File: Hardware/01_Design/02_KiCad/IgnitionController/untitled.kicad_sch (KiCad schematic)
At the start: 34 parts, among them Q4 PMOS-FET, Q5 BC856, Q6 IRF9Z34NSPbF, U3 LM2575-3.3BU, U4 LM2575-5.0BU, U9 LM2575-5.0BU

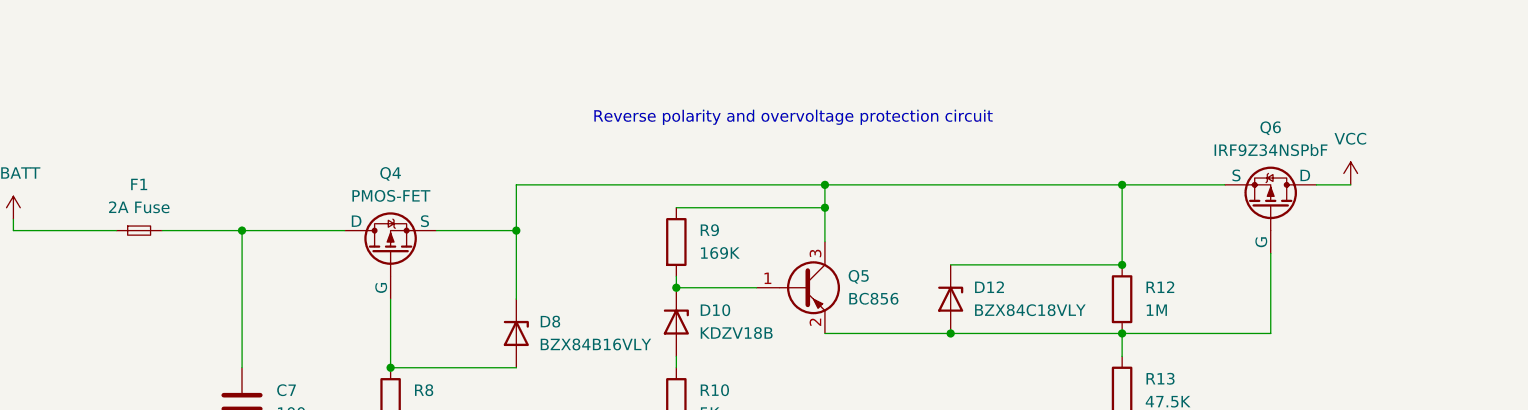
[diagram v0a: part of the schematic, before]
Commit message: Added Crystal to PMIC
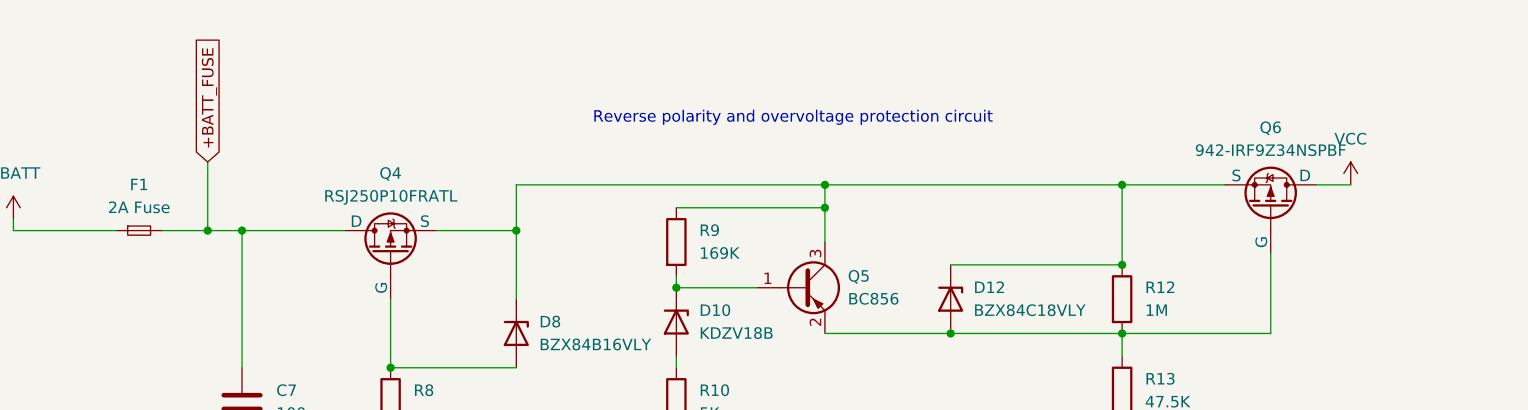
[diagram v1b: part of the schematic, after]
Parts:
- removed Q6: IRF9Z34NSPbF, Package_TO_SOT_SMD:TO-263-2, symbol Simulation_SPICE:PMOS
- added Q6: 942-IRF9Z34NSPBF, Library:TO-263-2_Transistor, symbol Library_sym.pretty:PMOS-FET
- C7: footprint Capacitor_SMD:C_0805_2012Metric_Pad1.18x1.45mm_HandSolder -> Capacitor_SMD:C_0603_1608Metric_Pad1.08x0.95mm_HandSolder
- Q4: value PMOS-FET -> RSJ250P10FRATL; Mouser PN (none) -> 755-RSJ250P10FRATL
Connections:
- net VCC: now also Q6.2 (D)
- net +BATT_FUSE: now reaches C7.1, F1.2, Q4.2 (D)
- net at D12.3 (K), D8.3 (K), Q4.3 (S)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: now also Q6.3 (S)
- net at D12.1 (A), Q5.2 (E), R12.2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: now also Q6.1 (G)
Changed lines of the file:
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@@
 	)
 	(junction
+		(at 67.31 53.34)
+		(diameter 0)
+		(color 0 0 0 0)
+	)
+	(junction
 		(at 168.91 57.15)
 		(diameter 0)
@@
 	(wire
 		(pts
+			(xy 67.31 53.34) (xy 62.23 53.34)
+		)
+		(stroke
+			(width 0)
+			(type default)
+		)
+	)
+	(wire
+		(pts
 			(xy 80.01 107.95) (xy 86.36 107.95)
 		)
@@
 	(wire
 		(pts
+			(xy 67.31 45.72) (xy 67.31 53.34)
+		)
+		(stroke
+			(width 0)
+			(type default)
+		)
+	)
+	(wire
+		(pts
 			(xy 31.75 111.76) (xy 31.75 115.57)
 		)
@@
 	(wire
 		(pts
-			(xy 71.12 53.34) (xy 62.23 53.34)
+			(xy 71.12 53.34) (xy 67.31 53.34)
 		)
 		(stroke
@@
 		)
 	)
+	(global_label "+BATT_FUSE"
+		(shape input)
+		(at 67.31 45.72 90)
+		(fields_autoplaced yes)
+		(effects
+			(font
+				(size 1.27 1.27)
+			)
+			(justify left)
+		)
+		(property "Intersheetrefs" "${INTERSHEET_REFS}"
+			(at 67.31 31.1234 90)
+			(effects
+				(font
+					(size 1.27 1.27)
+				)
+				(justify left)
+				(hide yes)
+			)
+		)
+	)
 	(symbol
 		(lib_id "Device:D_Zener")
@@
 			)
 		)
-		(property "Value" "PMOS-FET"
+		(property "Value" "RSJ250P10FRATL"
 			(at 87.63 49.53 90)
 			(effects
@@
 			)
 		)
+		(property "Mouser PN" "755-RSJ250P10FRATL"
+			(at 87.63 55.88 90)
+			(effects
+				(font
+					(size 1.27 1.27)
+				)
+				(hide yes)
+			)
+		)
 		(pin "3"
 		)
@@
 			)
 		)
-		(property "Footprint" "Capacitor_SMD:C_0805_2012Metric_Pad1.18x1.45mm_HandSolder"
+		(property "Footprint" "Capacitor_SMD:C_0603_1608Metric_Pad1.08x0.95mm_HandSolder"
 			(at 72.0852 76.2 0)
 			(effects
@@
 	)
 	(symbol
-		(lib_id "Simulation_SPICE:PMOS")
-		(at 185.42 50.8 270)
-		(mirror x)
-		(unit 1)
-		(exclude_from_sim no)
-		(in_bom yes)
-		(on_board yes)
-		(dnp no)
-		(property "Reference" "Q6"
-			(at 185.42 41.91 90)
-			(effects
-				(font
-					(size 1.27 1.27)
-				)
-			)
-		)
-		(property "Value" "IRF9Z34NSPbF"
-			(at 185.42 44.45 90)
-			(effects
-				(font
-					(size 1.27 1.27)
-				)
-			)
-		)
-		(property "Footprint" "Package_TO_SOT_SMD:TO-263-2"
-			(at 187.96 45.72 0)
-			(effects
-				(font
-					(size 1.27 1.27)
-				)
-				(hide yes)
-			)
-		)
-		(property "Datasheet" "https://ngspice.sourceforge.io/docs/ngspice-html-manual/manual.xhtml#cha_MOSFETs"
-			(at 172.72 50.8 0)
-			(effects
-				(font
-					(size 1.27 1.27)
-				)
-				(hide yes)
-			)
-		)
-		(property "Description" "P-MOSFET transistor, drain/source/gate"
-			(at 185.42 50.8 0)
-			(effects
-				(font
-					(size 1.27 1.27)
-				)
-				(hide yes)
-			)
-		)
-		(property "Sim.Device" "PMOS"
-			(at 168.275 50.8 0)
-			(effects
-				(font
-					(size 1.27 1.27)
-				)
-				(hide yes)
-			)
-		)
-		(property "Sim.Type" "VDMOS"
-			(at 166.37 50.8 0)
-			(effects
-				(font
-					(size 1.27 1.27)
-				)
-				(hide yes)
-			)
-		)
-		(property "Sim.Pins" "1=D 2=G 3=S"
-			(at 170.18 50.8 0)
-			(effects
-				(font
-					(size 1.27 1.27)
-				)
-				(hide yes)
-			)
-		)
-		(pin "2"
-		)
-		(pin "1"
-		)
-		(pin "3"
-		)
-		(instances
-			(project "IgnitionController"
-				(path "/96744ec0-1e7f-4d75-9985-0095978419e2/af36972c-908c-4a23-b0c1-8f51d47880c3"
-					(reference "Q6")
-					(unit 1)
-				)
-			)
-		)
-	)
-	(symbol
 		(lib_id "Diode:SS14")
 		(at 82.55 160.02 270)
@@
 					(unit 1)
 				)
+			)
+		)
+	)
+	(symbol
+		(lib_id "Library_sym.pretty:PMOS-FET")
+		(at 185.42 50.8 270)
+		(mirror x)
+		(unit 1)
+		(exclude_from_sim no)
+		(in_bom yes)
+		(on_board yes)
+		(dnp no)
+		(property "Reference" "Q6"
+			(at 185.42 41.91 90)
+			(effects
+				(font
+					(size 1.27 1.27)
+				)
+			)
+		)
+		(property "Value" "942-IRF9Z34NSPBF"
+			(at 185.42 44.45 90)
+			(effects
+				(font
+					(size 1.27 1.27)
+				)
+			)
+		)
+		(property "Footprint" "Library:TO-263-2_Transistor"
+			(at 187.96 45.72 0)
+			(effects
+				(font
+					(size 1.27 1.27)
+				)
+				(hide yes)
+			)
+		)
+		(property "Datasheet" "https://ngspice.sourceforge.io/docs/ngspice-html-manual/manual.xhtml#cha_MOSFETs"
+			(at 172.72 50.8 0)
+			(effects
+				(font
+					(size 1.27 1.27)
+				)
+				(hide yes)
+			)
+		)
+		(property "Description" "P-MOSFET transistor, drain/source/gate"
+			(at 185.42 50.8 0)
+			(effects
+				(font
+					(size 1.27 1.27)
+				)
+				(hide yes)
+			)
+		)
+		(property "Sim.Device" "PMOS"
+			(at 168.275 50.8 0)
+			(effects
+				(font
+					(size 1.27 1.27)
+				)
+				(hide yes)
+			)
+		)
+		(property "Sim.Type" "VDMOS"
+			(at 166.37 50.8 0)
+			(effects
+				(font
+					(size 1.27 1.27)
+				)
+				(hide yes)
+			)
+		)
+		(property "Sim.Pins" "1=D 2=G 3=S"
+			(at 170.18 50.8 0)
+			(effects
+				(font
+					(size 1.27 1.27)
+				)
+				(hide yes)
+			)
+		)
+		(property "Mouser PN" ""
+			(at 185.42 50.8 90)
+			(effects
+				(font
+					(size 1.27 1.27)
+				)
+				(hide yes)
+			)
+		)
+		(pin "3"
+		)
+		(pin "1"
+		)
+		(pin "2"
+		)
+		(instances
+			(project "IgnitionController"
+				(path "/96744ec0-1e7f-4d75-9985-0095978419e2/af36972c-908c-4a23-b0c1-8f51d47880c3"
+					(reference "Q6")
+					(unit 1)
+				)

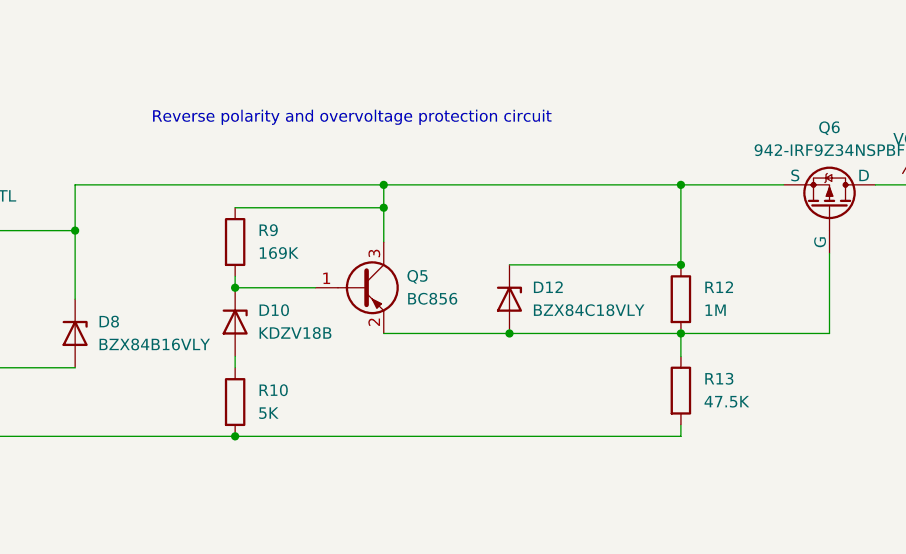
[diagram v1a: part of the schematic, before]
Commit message: Added Peripheral HW Components
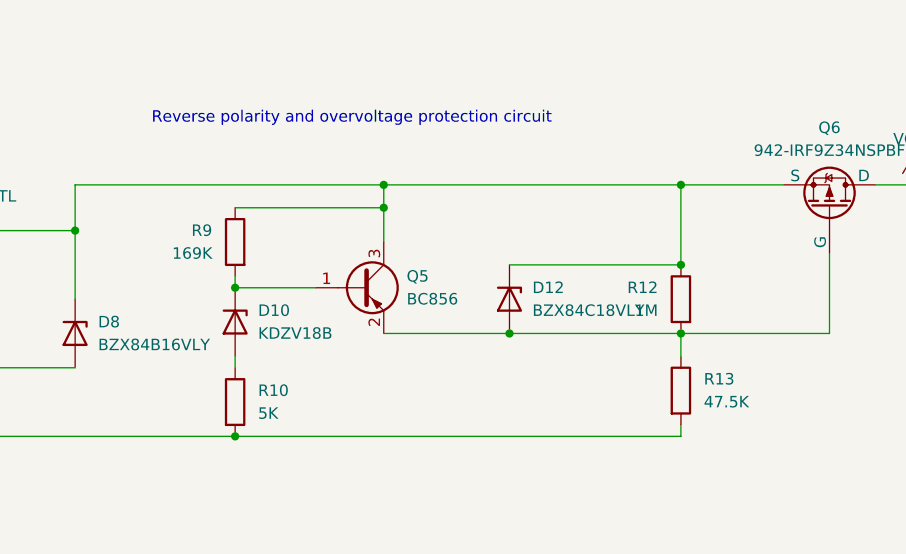
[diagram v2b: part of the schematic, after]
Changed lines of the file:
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@@
 		(lib_id "Device:R")
 		(at 168.91 60.96 0)
-		(unit 1)
-		(exclude_from_sim no)
-		(in_bom yes)
-		(on_board yes)
-		(dnp no)
-		(fields_autoplaced yes)
+		(mirror y)
+		(unit 1)
+		(exclude_from_sim no)
+		(in_bom yes)
+		(on_board yes)
+		(dnp no)
 		(property "Reference" "R12"
-			(at 171.45 59.6899 0)
+			(at 166.37 59.6899 0)
 			(effects
 				(font
@@
 		)
 		(property "Value" "1M"
-			(at 171.45 62.2299 0)
+			(at 166.37 62.2299 0)
 			(effects
 				(font
@@
 		)
 		(property "Footprint" "Resistor_SMD:R_0603_1608Metric_Pad0.98x0.95mm_HandSolder"
-			(at 167.132 60.96 90)
+			(at 170.688 60.96 90)
 			(effects
 				(font
@@
 		(lib_id "Device:R")
 		(at 119.38 54.61 0)
-		(unit 1)
-		(exclude_from_sim no)
-		(in_bom yes)
-		(on_board yes)
-		(dnp no)
-		(fields_autoplaced yes)
+		(mirror y)
+		(unit 1)
+		(exclude_from_sim no)
+		(in_bom yes)
+		(on_board yes)
+		(dnp no)
 		(property "Reference" "R9"
-			(at 121.92 53.3399 0)
+			(at 116.84 53.3399 0)
 			(effects
 				(font
@@
 		)
 		(property "Value" "169K"
-			(at 121.92 55.8799 0)
+			(at 116.84 55.8799 0)
 			(effects
 				(font
@@
 		)
 		(property "Footprint" "Resistor_SMD:R_0603_1608Metric_Pad0.98x0.95mm_HandSolder"
-			(at 117.602 54.61 90)
-			(effects
-				(font
+			(at 121.158 54.61 90)
+			(effects
+				(font
